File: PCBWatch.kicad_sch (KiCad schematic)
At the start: 36 parts, among them J1 Conn_01x05_Pin, J2 Touch Electrode, U1 STM32L010C6Tx, U2 MCP23017_SS, U3 AT42QT1010-TSHR, Y1 32.768KHZ

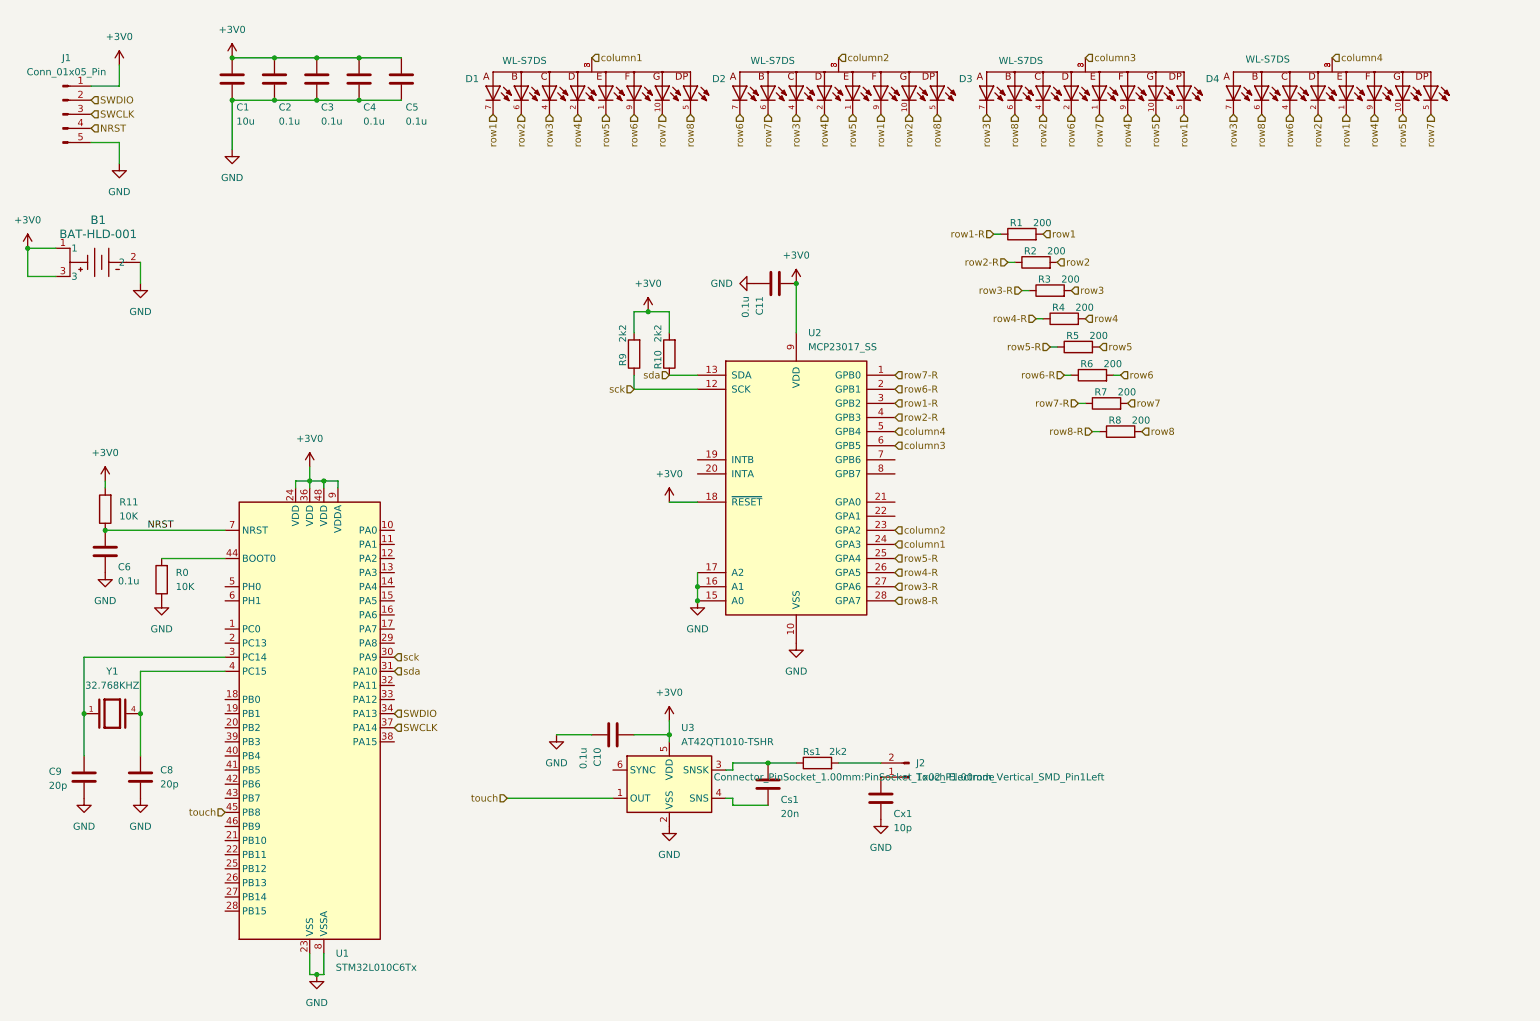
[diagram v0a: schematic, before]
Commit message: Two level board
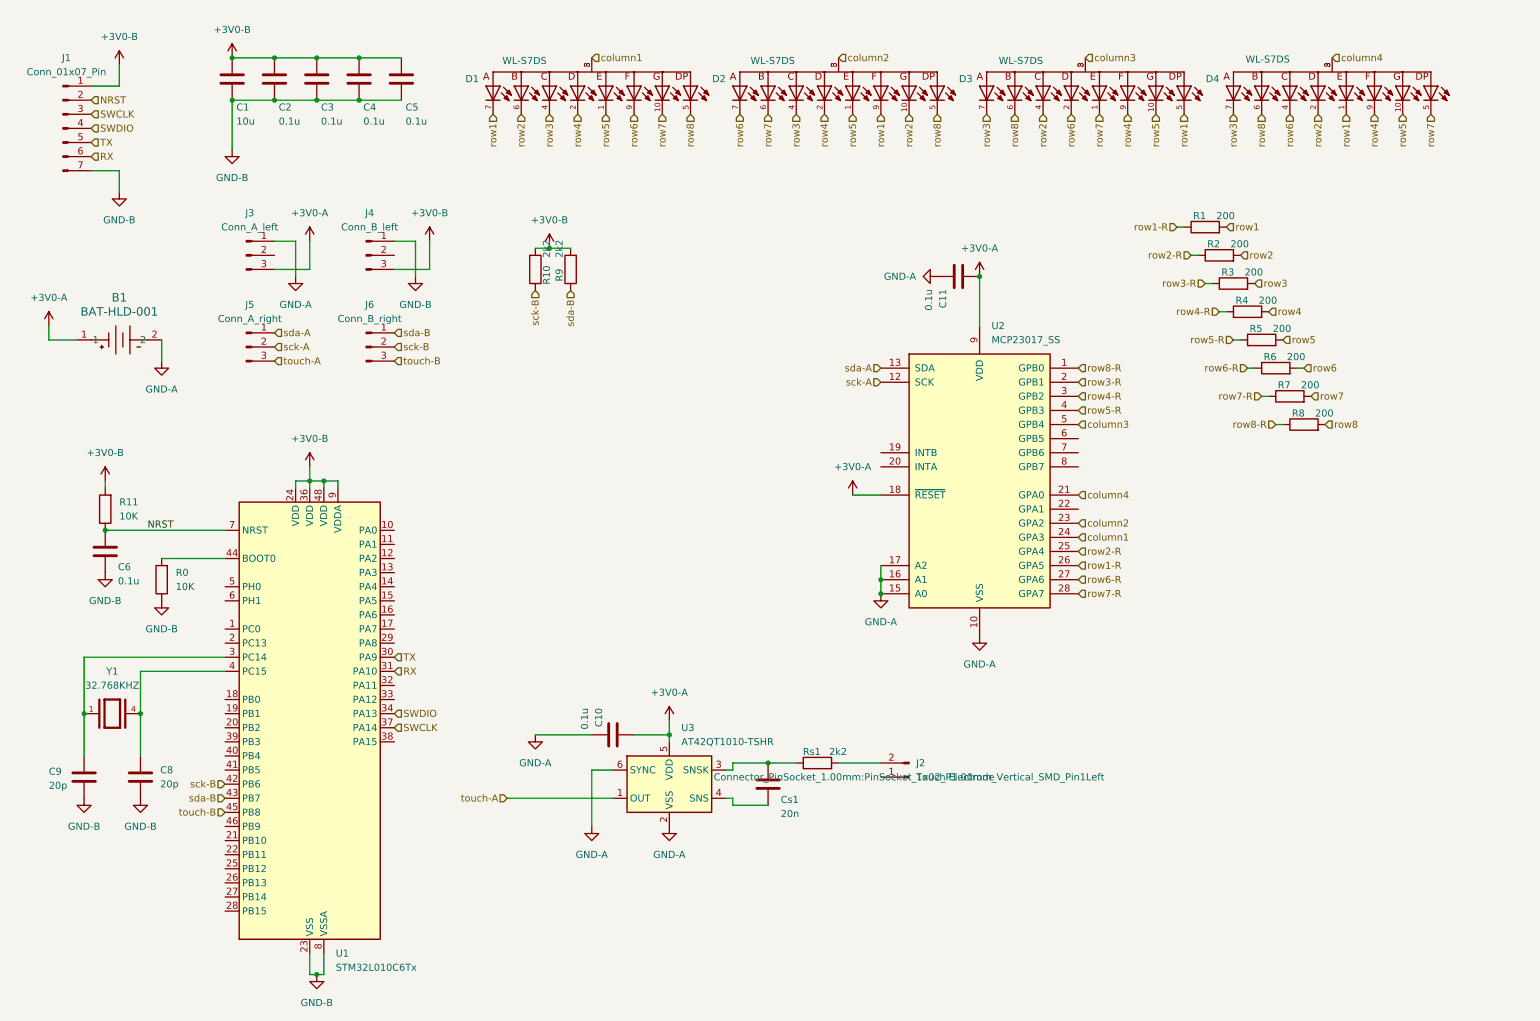
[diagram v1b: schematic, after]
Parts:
- removed Cx1: 10p, Capacitor_SMD:C_0805_2012Metric, symbol Device:C
- removed J1: Conn_01x05_Pin, my_footprints:SWD_pads, symbol Connector:Conn_01x05_Pin
- added J1: Conn_01x07_Pin, my_footprints:SWD_pads, symbol Connector:Conn_01x07_Pin
- added J3: Conn_A_left, Connector_PinHeader_1.27mm:PinHeader_1x03_P1.27mm_Vertical, symbol Connector:Conn_01x03_Pin
- added J4: Conn_B_left, my_footprints:3 Pin header socket, symbol Connector:Conn_01x03_Pin
- added J5: Conn_A_right, Connector_PinHeader_1.27mm:PinHeader_1x03_P1.27mm_Vertical, symbol Connector:Conn_01x03_Pin
- added J6: Conn_B_right, my_footprints:3 Pin header socket, symbol Connector:Conn_01x03_Pin
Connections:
- net NRST: now also J1.2 (Pin_2)
- net SWCLK: now also J1.3 (Pin_3)
- net SWDIO: now also J1.4 (Pin_4)
- net column3: now also U2.5 (GPB4); no longer U2.6 (GPB5)
- net column4: now also U2.21 (GPA0); no longer U2.5 (GPB4)
- net row1-R: now also U2.26 (GPA5); no longer U2.3 (GPB2)
- net row2-R: now also U2.25 (GPA4); no longer U2.4 (GPB3)
- net row3-R: now also U2.2 (GPB1); no longer U2.27 (GPA6)
- net row4-R: now also U2.3 (GPB2); no longer U2.26 (GPA5)
- net row5-R: now also U2.4 (GPB3); no longer U2.25 (GPA4)
- net row6-R: now also U2.27 (GPA6); no longer U2.2 (GPB1)
- net row7-R: now also U2.28 (GPA7); no longer U2.1 (GPB0)
- net row8-R: now also U2.1 (GPB0); no longer U2.28 (GPA7)
- net sck-B: now reaches U1.42 (PB6)
- net sck-B: now also R10.1, J6.2 (Pin_2)
- net sda-B: now reaches U1.43 (PB7)
- net sda-B: now also R9.1, J6.1 (Pin_1)
- net GND-A: now reaches U3.6 (SYNC)
- net GND-A: now also B1.2, C10.2, C11.2, U2.10 (VSS), U2.15 (A0), U2.16 (A1), U2.17 (A2), U3.2 (VSS), J3.1 (Pin_1)
- net +3V0 renamed +3V0-B
- net +3V0-B: now also J1.1 (Pin_1), J4.3 (Pin_3); no longer B1.1, B1.3, C10.1, C11.1, U2.18 (~{RESET}), U2.9 (VDD), U3.5 (VDD)
- net GND renamed GND-B
- net GND-B: now also J1.7 (Pin_7), J4.1 (Pin_1); no longer B1.2, C10.2, C11.2, U2.10 (VSS), U2.15 (A0), U2.16 (A1), U2.17 (A2), U3.2 (VSS)
- removed net sck: R9.1, U1.30 (PA9), U2.12 (SCK)
- removed net sda: R10.1, U1.31 (PA10), U2.13 (SDA)
- net touch renamed touch-A
- net touch-A: now also J5.3 (Pin_3); no longer U1.45 (PB8)
- new net +3V0-A: B1.1, C10.1, C11.1, J3.3 (Pin_3), U2.18 (~{RESET}), U2.9 (VDD), U3.5 (VDD)
- new net RX: J1.6 (Pin_6), U1.31 (PA10)
- new net TX: J1.5 (Pin_5), U1.30 (PA9)
- new net sck-A: J5.2 (Pin_2), U2.12 (SCK)
- new net sda-A: J5.1 (Pin_1), U2.13 (SDA)
- new net touch-B: J6.3 (Pin_3), U1.45 (PB8)
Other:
- moved on the sheet: C11, R1, R10, R2, R3, R4, R5, R6, R7, R8, R9, U2

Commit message: Push old changes of version 3
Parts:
- removed C10: 0.1u, Capacitor_SMD:C_0805_2012Metric, symbol Device:C
- removed Cs1: 20n, Capacitor_SMD:C_0805_2012Metric, symbol Device:C
- removed J2: Touch Electrode, Connector_PinSocket_1.00mm:PinSocket_1x02_P1.00mm_Vertical_SMD_Pin1Left, symbol Connector:Conn_01x02_Pin
- removed Rs1: 2k2, Resistor_SMD:R_0805_2012Metric, symbol Device:R
- removed U3: AT42QT1010-TSHR, Package_TO_SOT_SMD:SOT-23-6, symbol Sensor_Touch:AT42QT1010-TSHR
- added R12: 10K, Resistor_SMD:R_0805_2012Metric, symbol Device:R
- added SW1: SW_SPST, my_footprints:SKQYAAE010 Switch, symbol Switch:SW_SPST
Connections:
- net +3V0-A: now also SW1.2 (B)
- net GND-A: now also R12.1
- net touch-A: now also R12.2, SW1.1 (A)

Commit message: E-ink first idea
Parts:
- removed D1, D2, D3, D4: WL-S7DS, 7seg:WL-S7DS_0.3INCH, symbol WL-S7DS_0.3INCH_COMMON-ANODE:WL-S7DS_0.3INCH_COMMON-ANODE
- removed J3: Conn_A_left, Connector_PinHeader_1.27mm:PinHeader_1x03_P1.27mm_Vertical, symbol Connector:Conn_01x03_Pin
- removed J4: Conn_B_left, my_footprints:3 Pin header socket, symbol Connector:Conn_01x03_Pin
- removed J5: Conn_A_right, Connector_PinHeader_1.27mm:PinHeader_1x03_P1.27mm_Vertical, symbol Connector:Conn_01x03_Pin
- removed J6: Conn_B_right, my_footprints:3 Pin header socket, symbol Connector:Conn_01x03_Pin
- removed R1, R2, R3, R4, R7, R8: 200, Resistor_SMD:R_0805_2012Metric, symbol Device:R
- removed R10, R9: 2k2, Resistor_SMD:R_0805_2012Metric, symbol Device:R
- removed R12: 10K, Resistor_SMD:R_0805_2012Metric, symbol Device:R
- removed SW1: SW_SPST, my_footprints:SKQYAAE010 Switch, symbol Switch:SW_SPST
- removed U2: MCP23017_SS, Package_SO:SSOP-28_5.3x10.2mm_P0.65mm, symbol Interface_Expansion:MCP23017_SS
- added C10, C9: 4u7, Capacitor_SMD:C_0805_2012Metric, symbol Device:C
- added C12, C13, C14, C15, C16, C18, C19: 1u, Capacitor_SMD:C_0805_2012Metric, symbol Device:C
- added C17: 1u(optional), Capacitor_SMD:C_0805_2012Metric, symbol Device:C
- added D1, D2, D3: MBR0530, Diode_SMD:D_SOD-123, symbol Diode:MBR0530
- added J2: E-Ink connector, 24-Pin-FPC-Connector:AMPHENOL_SFV24R-1STE1HLF, symbol E-Ink:E-Ink-1.54-connector
- added L1: 10u/47u, LQH32CN100K23L:IND_LQH32CN100K23L, symbol Device:L
- added Q1: Si1304BDL / Si1308EDL TUBE MOS, Package_TO_SOT_SMD:SOT-323_SC-70_Handsoldering, symbol Simulation_SPICE:NMOS
- added e-ink1: ~, E-Ink-1.54:E-Ink 1.54 Display, symbol E-Ink-1.54:E-Ink_1.54_Display
- B1: footprint BATT_HLDR_LNX -> CR2032 Battery Holder:BATT_HLDR_LNX
- C1: renamed from C9; value 20p -> 10p
- C11: value 0.1u -> 1u
- C3: renamed from C8; value 20p -> 10p
- R5: value 200 -> 10k
- R6: value 200 -> 3/0.47/2.2
- renumbered C6 to C2, C1 to C4, C2 to C5, C3 to C6, C4 to C7, C5 to C8, R11 to R1, R0 to R2
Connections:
- net +3V0-B is gone; now on net +3V0: C4.1, C5.1, C6.1, C7.1, C8.1, J1.1 (Pin_1), R1.2, U1.24 (VDD), U1.36 (VDD), U1.48 (VDD), U1.9 (VDDA)
- net GND-B is gone; now on net GND: C1.2, C2.2, C3.2, C4.2, C5.2, C6.2, C7.2, C8.2, J1.7 (Pin_7), R2.1, U1.23 (VSS), U1.35 (VSS), U1.47 (VSS), U1.8 (VSSA)
- net row5-R is gone; now on net GND: R5.1
- net row6-R is gone; now on net GND: R6.1
- net CS: now reaches U1.14 (PA4)
- net CS: now also J2.12 (CS)
- net SCLK: now reaches U1.15 (PA5)
- net SCLK: now also J2.13 (SCL)
- net SDI: now reaches U1.17 (PA7)
- net SDI: now also J2.14 (SDA)
- net +3V0-A renamed +3V0
- net +3V0: now also C12.1, C9.1, J2.15 (VDDIO), J2.16 (VCI), L1.1; no longer C11.1
- net GND-A renamed GND
- net GND: now also C12.2, C13.2, C14.2, C15.2, C16.2, C17.2, C18.2, C19.2, C9.2, D2.1 (K), J2.17 (VSS), J2.8 (BS)
- net row5 renamed GDR
- net GDR: now also J2.2 (GDR), Q1.2 (G)
- net row6 renamed RESE
- net RESE: now also J2.3 (RESE), Q1.3 (S)
- net sck-B: no longer names the net of U1.42 (PB6)
- net sda-B: no longer names the net of U1.43 (PB7)
- net touch-B: no longer names the net of U1.45 (PB8)
- new net: C10.1, D1.1 (K), D2.2 (A)
- new net: C13.1, J2.18 (VDD)
- new net: C17.1, J2.19 (VPP)
- new net: C14.1, J2.20 (VSH1)
- new net: C15.1, J2.22 (VSL)
- new net: C16.1, J2.24 (VCOM)
- new net: C19.1, J2.5 (VSH2)
- new net: C10.2, D3.2 (A), L1.2, Q1.1 (D)
- new net BUSY: J2.9 (BUSY)
- new net D/C: J2.11 (D/C)
- new net PREVGH: C11.1, D3.1 (K), J2.21 (PREVGH)
- new net PREVGL: C18.1, D1.2 (A), J2.23 (PREVGL)
- new net RES: J2.10 (RES)

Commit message: Semi-finished rev4 pcb
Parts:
- removed J1: Conn_01x07_Pin, my_footprints:SWD_pads, symbol Connector:Conn_01x07_Pin
- added J1: UART Pads, my_footprints:Untitled_2, symbol Connector:Conn_01x03_Pin
- added J3: Pin header A, Connector_PinHeader_1.00mm:PinHeader_1x03_P1.00mm_Vertical, symbol Connector:Conn_01x03_Pin
- added J4: Pin header B, Connector_PinHeader_1.00mm:PinHeader_1x03_P1.00mm_Vertical, symbol Connector:Conn_01x03_Pin
- added J5: ~, PCB_USBC:PCBTypeC_14P, symbol PCB_USBC:PCBTypeC_14P
- added J6: Pin header A top, Connector_PinHeader_1.00mm:PinHeader_1x03_P1.00mm_Vertical, symbol Connector:Conn_01x03_Pin
- added J7: Pin header B top, Connector_PinHeader_1.00mm:PinHeader_1x03_P1.00mm_Vertical, symbol Connector:Conn_01x03_Pin
- added R3, R4, R7: 100K, Resistor_SMD:R_0805_2012Metric, symbol Device:R
- added S1, S2, S3: BUTTON, PTS526_SM15_SMTR2_LFS:PTS526SM15SMTR2LFS, symbol PTS526_SM15_SMTR2_LFS:PTS526_SM15_SMTR2_LFS
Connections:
- net +3V0: now also J3.1 (Pin_1), J5.B6 (DP2)
- net BUSY: now also U1.12 (PA2)
- net D/C: now also U1.13 (PA3)
- net GND: now also J2.SH1, J2.SH2, J1.3 (Pin_3), J3.3 (Pin_3), J5.B1 (GND)
- net NRST: now also J5.A5 (CC1)
- net RES: now also U1.11 (PA1)
- net RX: now also U1.43 (PB7), J1.2 (Pin_2); no longer U1.31 (PA10)
- net SWCLK: now also J5.B7 (DN2)
- net SWDIO: now also J5.A7 (DN1)
- net TX: now also U1.42 (PB6), J1.1 (Pin_1); no longer U1.30 (PA9)
- net BUTTON1: now reaches U1.20 (PB2)
- net BUTTON1: now also J4.2 (Pin_2)
- net BUTTON3: now reaches U1.21 (PB10)
- net BUTTON3: now also J4.3 (Pin_3)
- net BUTTON2: now reaches U1.22 (PB11)
- net BUTTON2: now also J4.1 (Pin_1)
- new net +3V0-T: J6.1 (Pin_1), S1.1, S1.2, S2.1, S2.2, S3.1, S3.2
- new net BUTTON1-T: J7.2 (Pin_2), R3.1, S1.3, S1.4
- new net BUTTON2-T: J7.1 (Pin_1), R4.1, S2.3, S2.4
- new net BUTTON3-T: J7.3 (Pin_3), R7.1, S3.3, S3.4
- new net GND-T: J6.3 (Pin_3), R3.2, R4.2, R7.2
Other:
- moved on the sheet: B1, C4, C5, C6, C7, C8, e-ink1

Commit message: Fix fpc pin ordering
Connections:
- net BUSY: now also U1.20 (PB2); no longer U1.12 (PA2)
- net BUTTON1: now also U1.22 (PB11); no longer U1.20 (PB2)
- net BUTTON2: now also U1.21 (PB10); no longer U1.22 (PB11)
- net BUTTON3: now also U1.11 (PA1); no longer U1.21 (PB10)
- net D/C: now also U1.18 (PB0); no longer U1.13 (PA3)
- net RES: now also U1.19 (PB1); no longer U1.11 (PA1)

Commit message: Add prevgh prevgl testpoints
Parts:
- L1: value 10u/47u -> UC:10uH,1A SSD:/47uH, 0.5mA
- Q1: value Si1304BDL / Si1308EDL TUBE MOS -> Si1304BDL / Si1308EDL TUBE MOS / AO3400
- R6: value 3/0.47/2.2 -> 2.2 (ew. 3/0.47)
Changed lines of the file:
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@@
 		(dnp no)
 		(property "Reference" "R6"
-			(at 144.272 99.822 90)
+			(at 152.146 97.79 0)
 			(effects
 				(font
@@
 			)
 		)
-		(property "Value" "3/0.47/2.2"
-			(at 146.304 94.488 90)
+		(property "Value" "2.2 (ew. 3/0.47)"
+			(at 150.368 99.822 0)
 			(do_not_autoplace yes)
 			(effects
@@
 					(size 1.27 1.27)
 				)
-				(justify left)
+				(justify right)
 			)
 		)
@@
 			)
 		)
-		(property "Value" "10u/47u"
+		(property "Value" "UC:10uH,1A SSD:/47uH, 0.5mA"
 			(at 139.7 64.77 90)
 			(effects
@@
 			)
 		)
-		(property "Value" "Si1304BDL / Si1308EDL TUBE MOS"
+		(property "Value" "Si1304BDL / Si1308EDL TUBE MOS / AO3400"
 			(at 152.4 90.1699 0)
 			(effects
